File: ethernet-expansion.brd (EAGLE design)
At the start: 64.4 x 50.8 mm, 22 parts, among them Q1 25MHz, U1 ENC28J60-SO

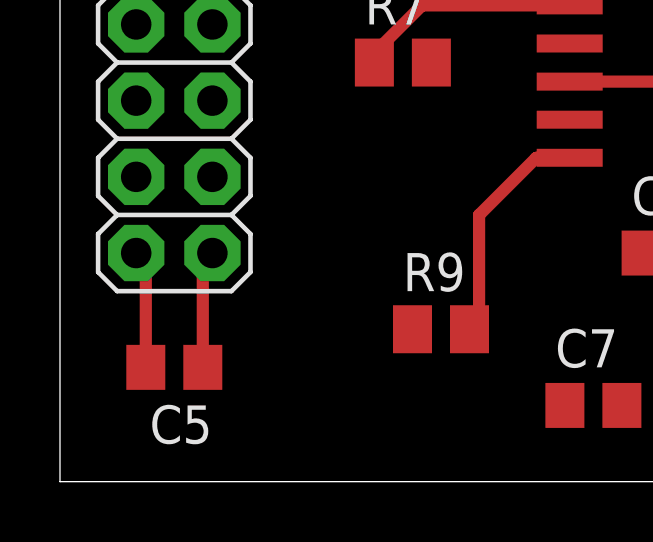
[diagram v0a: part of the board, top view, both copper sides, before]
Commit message: Add center tap connection and interrupt connections
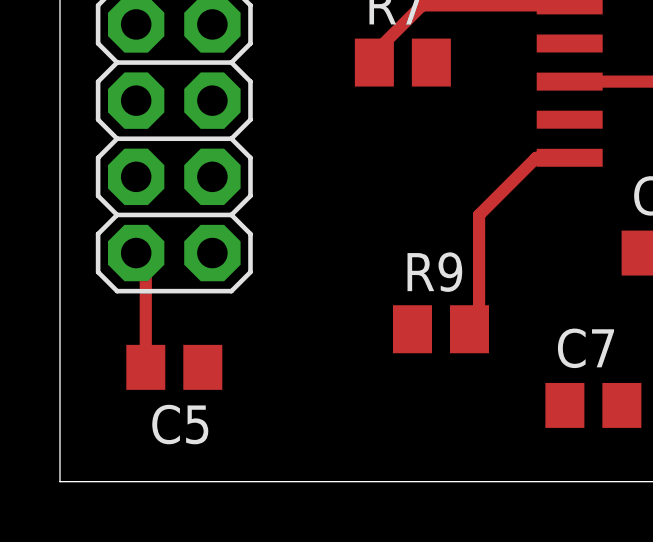
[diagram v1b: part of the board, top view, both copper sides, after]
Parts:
- C10, C5, C7, C8, C9: value 100nF -> 0.1uF
- C4, C6: value 0.01uF -> 0.1uF
- R1, R2, R3, R4: value 50 -> 49.9
- R9: value 2K -> 2.32K
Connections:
- net +3V3: now also RJ1.P4
- net ETH_INT0: now also JP1.9
- net ETH_INT1: now also JP1.7
- net GND: now also RJ1.GND
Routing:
- net +3V3: track 3.94 -> 0.45 mm
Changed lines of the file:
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@@
 </autorouter>
 <elements>
-<element name="C4" library="resistor" package="C0805" value="0.01uF" x="33.02" y="19.05"/>
-<element name="C6" library="resistor" package="C0805" value="0.01uF" x="46.99" y="2.54"/>
+<element name="C4" library="resistor" package="C0805" value="0.1uF" x="33.02" y="19.05"/>
+<element name="C6" library="resistor" package="C0805" value="0.1uF" x="46.99" y="2.54"/>
 <element name="C1" library="resistor" package="C0805" value="10pF" x="24.13" y="39.37"/>
 <element name="C2" library="resistor" package="C0805" value="10pF" x="19.05" y="39.37" rot="R180"/>
-<element name="C5" library="resistor" package="C0805" value="100nF" x="3.81" y="3.81" rot="R180"/>
+<element name="C5" library="resistor" package="C0805" value="0.1uF" x="3.81" y="3.81" rot="R180"/>
 <element name="C3" library="resistor" package="C0805" value="10uF" x="12.7" y="33.02"/>
 <element name="JP1" library="SparkFun-Connectors" package="2X10" value="" x="3.81" y="19.05" rot="R270"/>
@@
 <attribute name="OC_FARNELL" value="1667008" x="21.59" y="34.29" size="1.778" layer="27" rot="R180" display="off"/>
 </element>
-<element name="R1" library="resistor" package="M0805" value="50" x="34.29" y="10.16"/>
-<element name="R2" library="resistor" package="M0805" value="50" x="36.83" y="12.7"/>
-<element name="R3" library="resistor" package="M0805" value="50" x="40.64" y="16.51"/>
-<element name="R4" library="resistor" package="M0805" value="50" x="39.37" y="6.35"/>
+<element name="R1" library="resistor" package="M0805" value="49.9" x="34.29" y="10.16"/>
+<element name="R2" library="resistor" package="M0805" value="49.9" x="36.83" y="12.7"/>
+<element name="R3" library="resistor" package="M0805" value="49.9" x="40.64" y="16.51"/>
+<element name="R4" library="resistor" package="M0805" value="49.9" x="39.37" y="6.35"/>
 <element name="R5" library="resistor" package="M0805" value="330" x="48.26" y="25.4"/>
 <element name="R6" library="resistor" package="M0805" value="330" x="54.61" y="27.94"/>
 <element name="R7" library="resistor" package="M0805" value="10K" x="11.43" y="13.97"/>
-<element name="R9" library="resistor" package="M0805" value="2K" x="12.7" y="5.08"/>
+<element name="R9" library="resistor" package="M0805" value="2.32K" x="12.7" y="5.08"/>
 <element name="U1" library="microchip-enc28j60" package="SO28W" value="ENC28J60-SO" x="21.59" y="19.05" rot="R270"/>
 <element name="RJ1" library="CONNECTER" package="HR911105A" value="HR911105A" x="55.88" y="13.97"/>
-<element name="C7" library="resistor" package="C0805" value="100nF" x="17.78" y="2.54"/>
-<element name="C8" library="resistor" package="C0805" value="100nF" x="26.67" y="2.54"/>
-<element name="C9" library="resistor" package="C0805" value="100nF" x="33.02" y="2.54"/>
-<element name="C10" library="resistor" package="C0805" value="100nF" x="20.32" y="7.62"/>
+<element name="C7" library="resistor" package="C0805" value="0.1uF" x="17.78" y="2.54"/>
+<element name="C8" library="resistor" package="C0805" value="0.1uF" x="26.67" y="2.54"/>
+<element name="C9" library="resistor" package="C0805" value="0.1uF" x="33.02" y="2.54"/>
+<element name="C10" library="resistor" package="C0805" value="0.1uF" x="20.32" y="7.62"/>
 </elements>
 <signals>
@@
 <contactref element="C4" pad="1"/>
 <contactref element="R7" pad="2"/>
-<contactref element="C5" pad="1"/>
-<contactref element="U1" pad="28"/>
 <contactref element="JP1" pad="20"/>
 <wire x1="5.08" y1="7.62" x2="4.76" y2="7.3" width="0.4064" layer="1"/>
-<wire x1="4.76" y1="7.3" x2="4.76" y2="3.81" width="0.4064" layer="1"/>
-<contactref element="U1" pad="25"/>
-<contactref element="C7" pad="1"/>
-<contactref element="C8" pad="1"/>
-<contactref element="U1" pad="15"/>
 <contactref element="C9" pad="1"/>
 <contactref element="U1" pad="20"/>
+<contactref element="U1" pad="28"/>
+<contactref element="C8" pad="1"/>
+<contactref element="U1" pad="25"/>
+<contactref element="U1" pad="15"/>
+<contactref element="C10" pad="1"/>
 <contactref element="U1" pad="19"/>
-<contactref element="C10" pad="1"/>
-<wire x1="26.19" y1="23.495" x2="26.19" y2="27.305" width="0" layer="19" extent="1-1"/>
-<wire x1="26.19" y1="17.145" x2="26.19" y2="23.495" width="0" layer="19" extent="1-1"/>
-<wire x1="26.19" y1="15.875" x2="26.19" y2="17.145" width="0" layer="19" extent="1-1"/>
-<wire x1="26.19" y1="10.795" x2="26.19" y2="15.875" width="0" layer="19" extent="1-1"/>
+<contactref element="C5" pad="1"/>
+<contactref element="C7" pad="1"/>
+<contactref element="RJ1" pad="P4"/>
+<wire x1="37.78" y1="12.7" x2="46.99" y2="13.335" width="0" layer="19" extent="1-1"/>
+<wire x1="35.24" y1="10.16" x2="37.78" y2="12.7" width="0" layer="19" extent="1-1"/>
+<wire x1="32.07" y1="2.54" x2="35.24" y2="10.16" width="0" layer="19" extent="1-1"/>
+<wire x1="25.72" y1="2.54" x2="32.07" y2="2.54" width="0" layer="19" extent="1-1"/>
+<wire x1="19.37" y1="7.62" x2="25.72" y2="2.54" width="0" layer="19" extent="1-1"/>
+<wire x1="16.83" y1="2.54" x2="19.37" y2="7.62" width="0" layer="19" extent="1-1"/>
+<wire x1="26.19" y1="10.795" x2="19.37" y2="7.62" width="0" layer="19" extent="1-1"/>
+<wire x1="26.19" y1="15.875" x2="26.19" y2="10.795" width="0" layer="19" extent="1-1"/>
+<wire x1="26.19" y1="17.145" x2="26.19" y2="15.875" width="0" layer="19" extent="1-1"/>
 <wire x1="32.07" y1="19.05" x2="26.19" y2="17.145" width="0" layer="19" extent="1-1"/>
-<wire x1="19.37" y1="7.62" x2="26.19" y2="10.795" width="0" layer="19" extent="1-1"/>
-<wire x1="16.83" y1="2.54" x2="19.37" y2="7.62" width="0" layer="19" extent="1-1"/>
-<wire x1="25.72" y1="2.54" x2="19.37" y2="7.62" width="0" layer="19" extent="1-1"/>
-<wire x1="32.07" y1="2.54" x2="25.72" y2="2.54" width="0" layer="19" extent="1-1"/>
-<wire x1="35.24" y1="10.16" x2="32.07" y2="2.54" width="0" layer="19" extent="1-1"/>
-<wire x1="37.78" y1="12.7" x2="35.24" y2="10.16" width="0" layer="19" extent="1-1"/>
+<wire x1="26.19" y1="23.495" x2="26.19" y2="17.145" width="0" layer="19" extent="1-1"/>
+<wire x1="26.19" y1="27.305" x2="26.19" y2="23.495" width="0" layer="19" extent="1-1"/>
 <wire x1="12.38" y1="13.97" x2="19.37" y2="7.62" width="0" layer="19" extent="1-1"/>
 <wire x1="5.08" y1="7.62" x2="12.38" y2="13.97" width="0" layer="19" extent="1-1"/>
+<wire x1="4.76" y1="3.81" x2="4.76" y2="7.3" width="0" layer="19" extent="1-1"/>
 </signal>
 <signal name="GND">
@@
 <contactref element="RJ1" pad="Y-"/>
 <contactref element="RJ1" pad="G-"/>
+<contactref element="RJ1" pad="GND"/>
 <wire x1="60.833" y1="9.906" x2="60.833" y2="18.034" width="0" layer="19" extent="1-1"/>
-<wire x1="47.94" y1="2.54" x2="60.833" y2="9.906" width="0" layer="19" extent="1-1"/>
-<wire x1="33.97" y1="2.54" x2="47.94" y2="2.54" width="0" layer="19" extent="1-1"/>
-<wire x1="27.62" y1="2.54" x2="33.97" y2="2.54" width="0" layer="19" extent="1-1"/>
-<wire x1="21.27" y1="7.62" x2="27.62" y2="2.54" width="0" layer="19" extent="1-1"/>
+<wire x1="46.99" y1="18.415" x2="60.833" y2="18.034" width="0" layer="19" extent="1-1"/>
+<wire x1="33.97" y1="19.05" x2="46.99" y2="18.415" width="0" layer="19" extent="1-1"/>
+<wire x1="26.19" y1="18.415" x2="33.97" y2="19.05" width="0" layer="19" extent="1-1"/>
+<wire x1="26.19" y1="19.685" x2="26.19" y2="18.415" width="0" layer="19" extent="1-1"/>
+<wire x1="26.19" y1="14.605" x2="26.19" y2="18.415" width="0" layer="19" extent="1-1"/>
+<wire x1="21.27" y1="7.62" x2="26.19" y2="14.605" width="0" layer="19" extent="1-1"/>
 <wire x1="18.73" y1="2.54" x2="21.27" y2="7.62" width="0" layer="19" extent="1-1"/>
 <wire x1="11.75" y1="5.08" x2="18.73" y2="2.54" width="0" layer="19" extent="1-1"/>
+<wire x1="27.62" y1="2.54" x2="21.27" y2="7.62" width="0" layer="19" extent="1-1"/>
+<wire x1="33.97" y1="2.54" x2="27.62" y2="2.54" width="0" layer="19" extent="1-1"/>
 <wire x1="16.99" y1="14.605" x2="21.27" y2="7.62" width="0" layer="19" extent="1-1"/>
-<wire x1="26.19" y1="14.605" x2="21.27" y2="7.62" width="0" layer="19" extent="1-1"/>
-<wire x1="26.19" y1="18.415" x2="26.19" y2="14.605" width="0" layer="19" extent="1-1"/>
-<wire x1="26.19" y1="19.685" x2="26.19" y2="18.415" width="0" layer="19" extent="1-1"/>
-<wire x1="33.97" y1="19.05" x2="26.19" y2="18.415" width="0" layer="19" extent="1-1"/>
 <wire x1="2.86" y1="3.81" x2="11.75" y2="5.08" width="0" layer="19" extent="1-1"/>
 <wire x1="16.99" y1="26.035" x2="26.19" y2="19.685" width="0" layer="19" extent="1-1"/>
@@
 <wire x1="18.1" y1="39.37" x2="13.65" y2="33.02" width="0" layer="19" extent="1-1"/>
 <wire x1="25.08" y1="39.37" x2="18.1" y2="39.37" width="0" layer="19" extent="1-1"/>
+<wire x1="47.94" y1="2.54" x2="33.97" y2="2.54" width="0" layer="19" extent="1-1"/>
 </signal>
 <signal name="N$8">
@@
 <signal name="ETH_INT0">
 <contactref element="U1" pad="4"/>
+<contactref element="JP1" pad="9"/>
+<wire x1="2.54" y1="20.32" x2="16.99" y2="23.495" width="0" layer="19" extent="1-1"/>
 </signal>
 <signal name="ETH_CLK">
@@
 <signal name="ETH_INT1">
 <contactref element="U1" pad="5"/>
+<contactref element="JP1" pad="7"/>
+<wire x1="2.54" y1="22.86" x2="16.99" y2="22.225" width="0" layer="19" extent="1-1"/>
 </signal>
 <signal name="N$9">

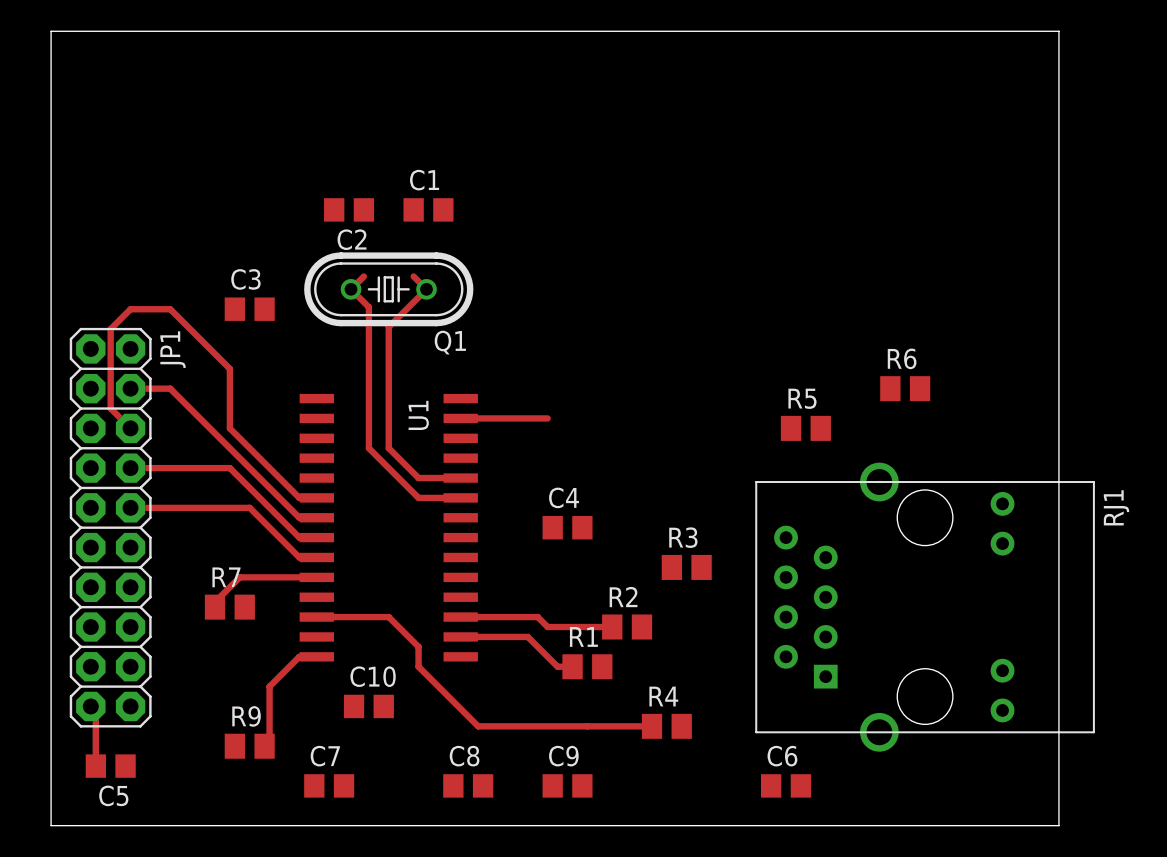
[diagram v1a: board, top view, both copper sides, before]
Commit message: Started to route the connector
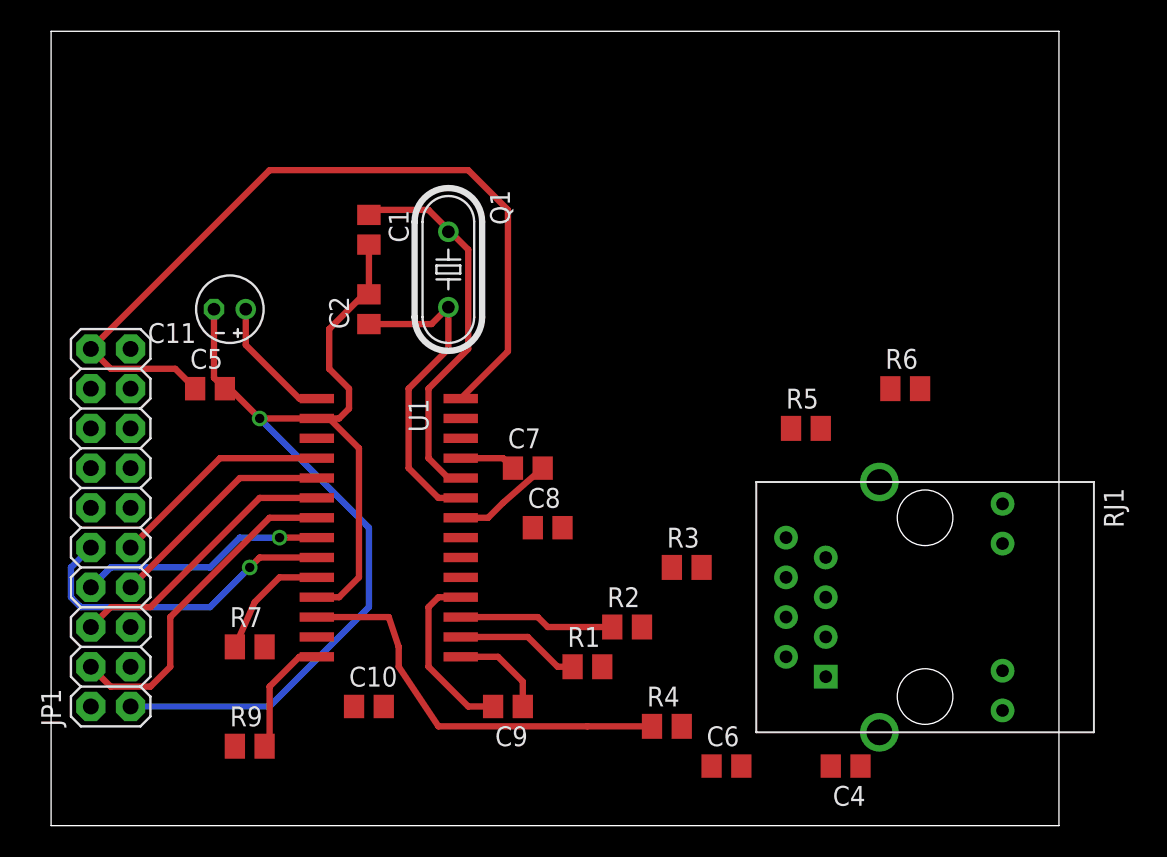
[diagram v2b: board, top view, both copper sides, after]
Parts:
- removed C3: 10uF, resistor:C0805
- added C11: 10uF, resistor:E2-4
- moved C5 25.0 mm to (10.2, 27.9), turned to 0 degrees
- moved C7 24.0 mm to (30.5, 22.9)
- moved C4 23.4 mm to (50.8, 3.81), turned to 180 degrees
- moved C8 17.3 mm to (31.8, 19.1)
- moved C2 6.48 mm to (20.3, 33.0), turned to 90 degrees
- moved C9 6.35 mm to (29.2, 7.62), turned to 180 degrees
- moved C6 4.02 mm to (43.2, 3.81)
- moved Q1 4.02 mm to (25.4, 35.6), turned to 270 degrees
- moved C1 4.02 mm to (20.3, 38.1), turned to 270 degrees
- moved R7 2.84 mm to (12.7, 11.4)
- turned JP1 to 90 degrees
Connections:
- net GND: now also C11.-, JP1.1; no longer C3.2, JP1.19
- net N$14: now also C11.+; no longer C3.1
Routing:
- net GND: track 3.94 -> 91.4 mm, vias 0 -> 1
- net +3V3: track 0.45 -> 63.3 mm
- net ETH_INT1: track 0.00 -> 14.8 mm
- net ETH_INT0: track 0.00 -> 14.3 mm
- net ETH_MISO: track 27.8 -> 17.9 mm
- net N$14: track 0.00 -> 8.25 mm
- net ETH_CS: track 13.2 -> 21.0 mm, vias 0 -> 1
- net N$11: track 17.7 -> 24.6 mm
- net ETH_MOSI: track 15.3 -> 21.3 mm
- net GREEN: track 5.56 -> 0.00 mm
- net ETH_CLK: track 13.8 -> 15.8 mm, vias 0 -> 1
- net N$12: track 19.0 -> 21.0 mm
- net N$4: track 20.9 -> 22.0 mm

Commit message: Initial board with all wires routed
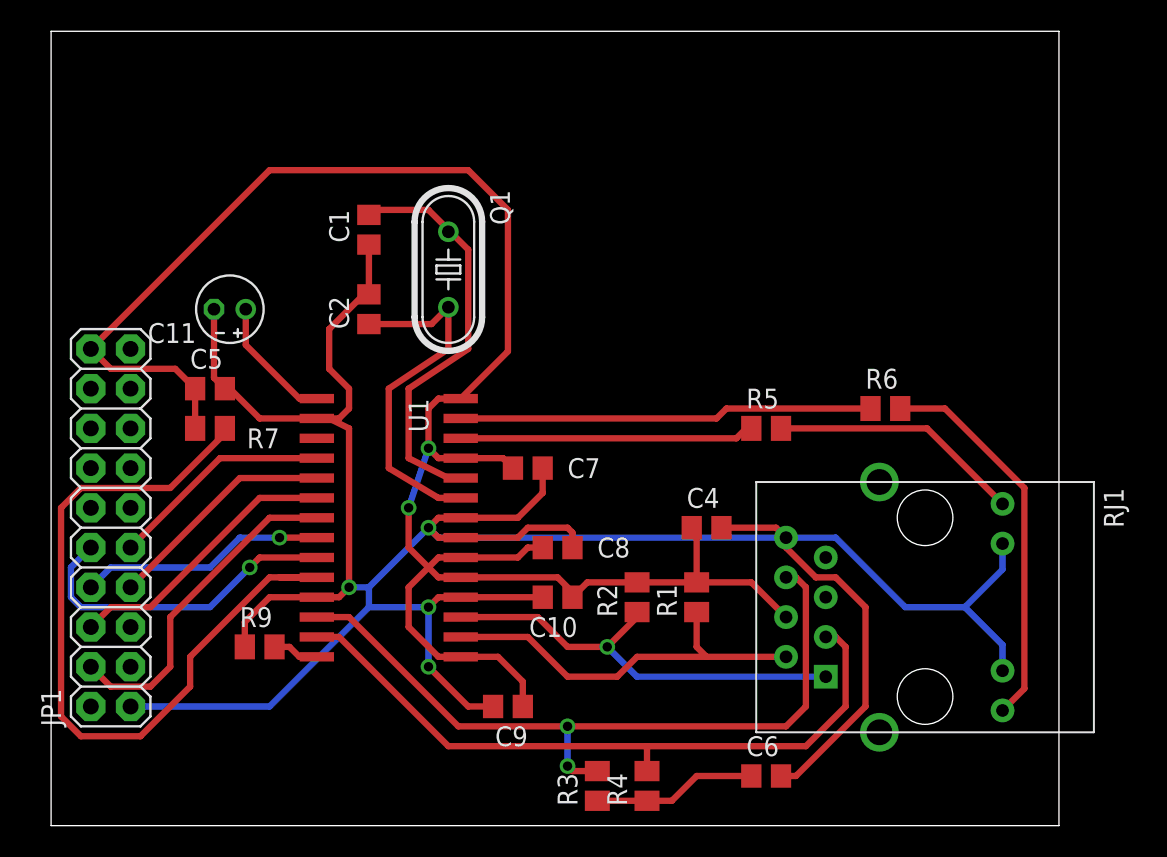
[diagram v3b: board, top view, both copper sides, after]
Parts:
- moved C4 17.6 mm to (41.9, 19.1), turned to 0 degrees
- moved R3 15.1 mm to (34.9, 2.54), turned to 90 degrees
- moved R7 14.2 mm to (10.2, 25.4), turned to 180 degrees
- moved C10 13.9 mm to (32.4, 14.6), turned to 180 degrees
- moved R1 8.28 mm to (41.3, 14.6), turned to 90 degrees
- moved R9 6.38 mm to (13.3, 11.4)
- moved R4 4.02 mm to (38.1, 2.54), turned to 90 degrees
- moved C6 2.62 mm to (45.7, 3.17)
- moved R5 2.54 mm to (45.7, 25.4)
- moved R2 2.01 mm to (37.5, 14.6), turned to 90 degrees
- moved R6 1.80 mm to (53.3, 26.7)
- moved C8 1.42 mm to (32.4, 17.8)
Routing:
- net GND: track 91.4 -> 186.0 mm, vias 1 -> 4
- net +3V3: track 63.3 -> 126.5 mm, vias 0 -> 2
- net N$3: track 0.00 -> 44.7 mm
- net N$16: track 7.76 -> 50.7 mm
- net GREEN: track 0.00 -> 26.5 mm
- net N$4: track 22.0 -> 48.4 mm, vias 0 -> 2
- net N$10: track 0.00 -> 24.8 mm
- net YELLOW: track 0.00 -> 18.8 mm
- net N$1: track 9.95 -> 27.9 mm, vias 0 -> 1
- net N$2: track 7.94 -> 25.5 mm
- net N$9: track 0.00 -> 16.2 mm
- net N$8: track 4.13 -> 10.5 mm
- net N$13: track 7.75 -> 2.97 mm
- net N$11: track 24.6 -> 26.6 mm
- net N$12: track 21.0 -> 23.0 mm

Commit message: Adding some text
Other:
- board size 64.4 x 50.8 mm -> 64.4 x 44.4 mm
- board text added: "Ethernet Module Version 1.0"
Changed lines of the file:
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@@
 <plain>
 <wire x1="0" y1="0" x2="64.44" y2="0" width="0" layer="20"/>
-<wire x1="64.44" y1="0" x2="64.44" y2="50.79" width="0" layer="20"/>
-<wire x1="64.44" y1="50.79" x2="0" y2="50.79" width="0" layer="20"/>
-<wire x1="0" y1="50.79" x2="0" y2="0" width="0" layer="20"/>
+<wire x1="64.44" y1="0" x2="64.44" y2="44.44" width="0" layer="20"/>
+<wire x1="64.44" y1="44.44" x2="0" y2="44.44" width="0" layer="20"/>
+<wire x1="0" y1="44.44" x2="0" y2="0" width="0" layer="20"/>
+<text x="35.56" y="33.02" size="1.778" layer="1">Ethernet Module
+Version 1.0</text>
 </plain>
 <attributes>
@@
 </board>
 </drawing>
+<compatibility>
+<note version="6.3" minversion="6.2.2" severity="warning">
+Since Version 6.2.2 text objects can contain more than one line,
+which will not be processed correctly with this version.
+</note>
+</compatibility>
 </eagle>
